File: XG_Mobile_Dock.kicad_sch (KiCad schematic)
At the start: 24 parts, among them J1 5-1775443-8, J2 20455-040E-76, J3 20455-040E-76, J4 3-2362375-4, J7 Conn_02x10_Odd_Even, J8 Conn_02x10_Odd_Even

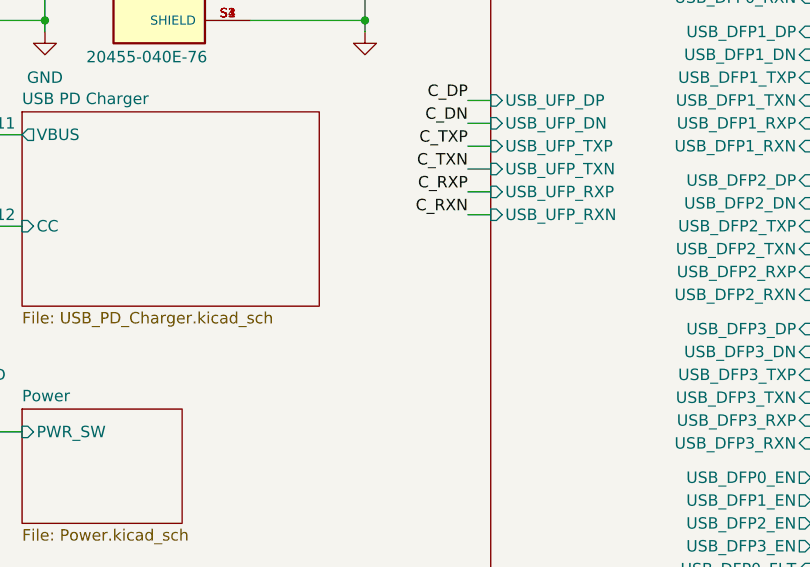
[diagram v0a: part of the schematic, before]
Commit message: Add TPS65987D charger circuit
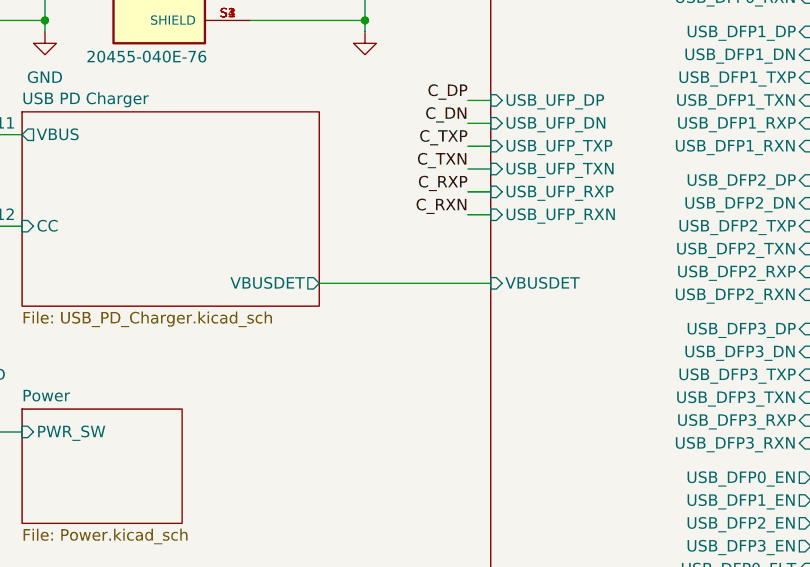
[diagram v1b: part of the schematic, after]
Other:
- sheet USB Hub ports: added VBUSDET; removed none
- sheet USB PD Charger ports: added VBUSDET; removed none
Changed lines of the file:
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@@
 	(wire
 		(pts
+			(xy 77.47 152.4) (xy 96.52 152.4)
+		)
+		(stroke
+			(width 0)
+			(type default)
+		)
+	)
+	(wire
+		(pts
 			(xy 82.55 123.19) (xy 82.55 124.46)
 		)
@@
 			)
 		)
+		(pin "VBUSDET" input
+			(at 96.52 152.4 180)
+			(effects
+				(font
+					(size 1.27 1.27)
+				)
+				(justify left)
+			)
+		)
 		(instances
 			(project "XG_Mobile_Dock"
@@
 			)
 		)
+		(pin "VBUSDET" output
+			(at 77.47 152.4 0)
+			(effects
+				(font
+					(size 1.27 1.27)
+				)
+				(justify right)
+			)
+		)

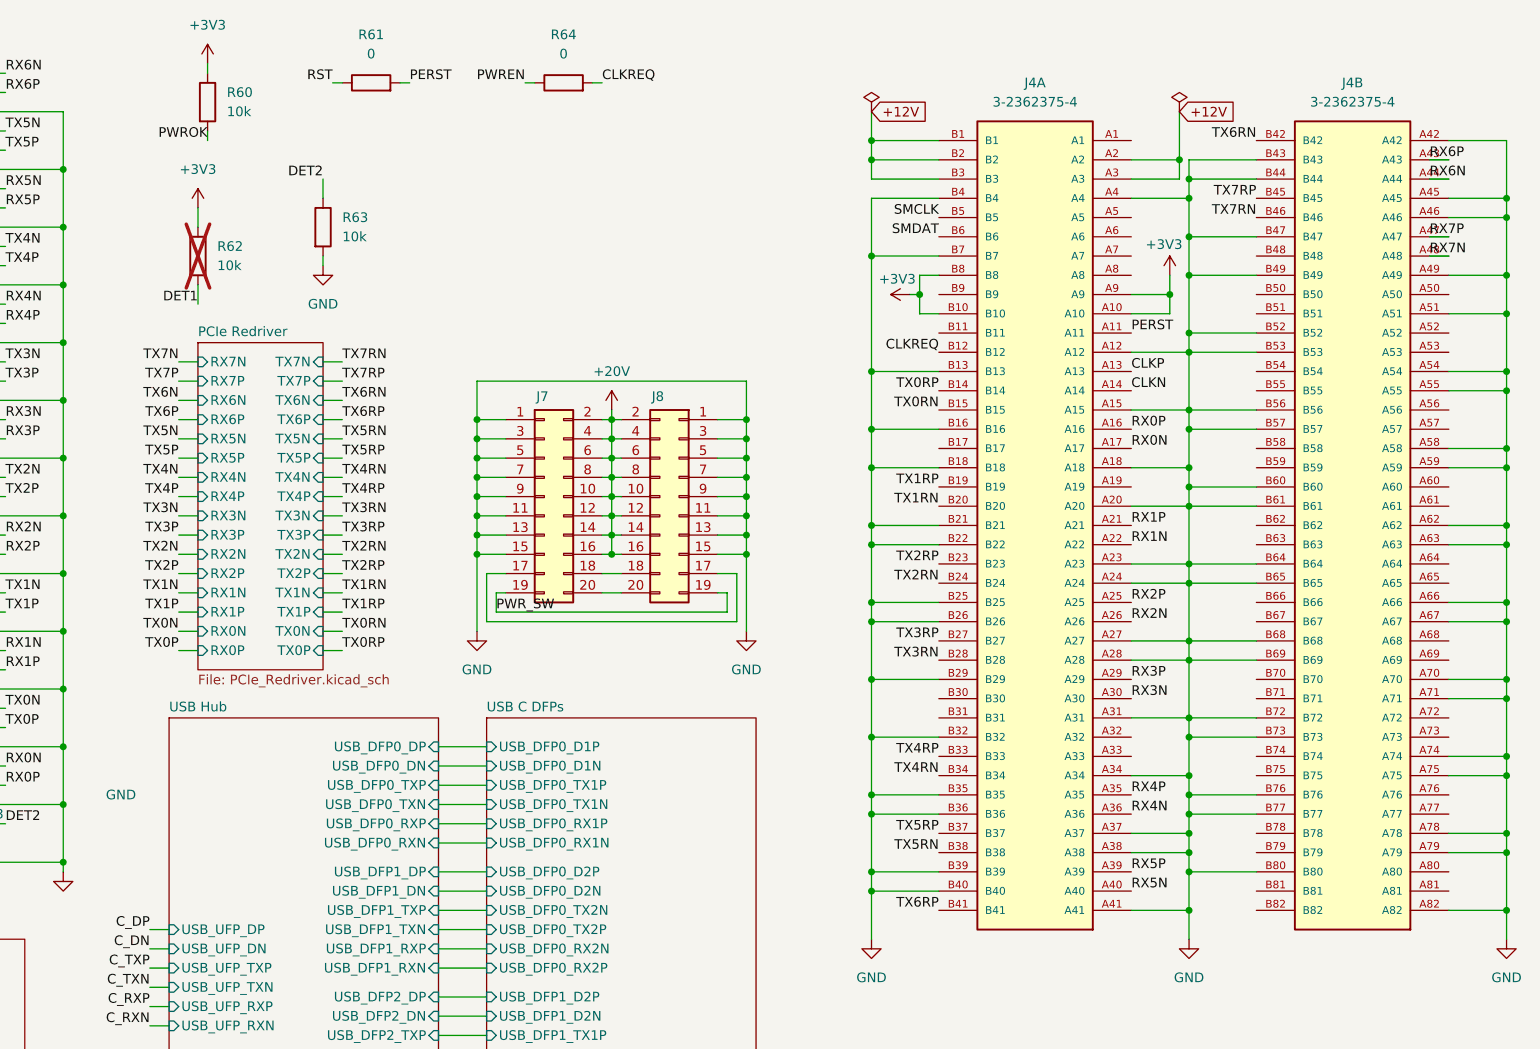
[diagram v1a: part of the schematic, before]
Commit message: Rewired PCIe without redriver
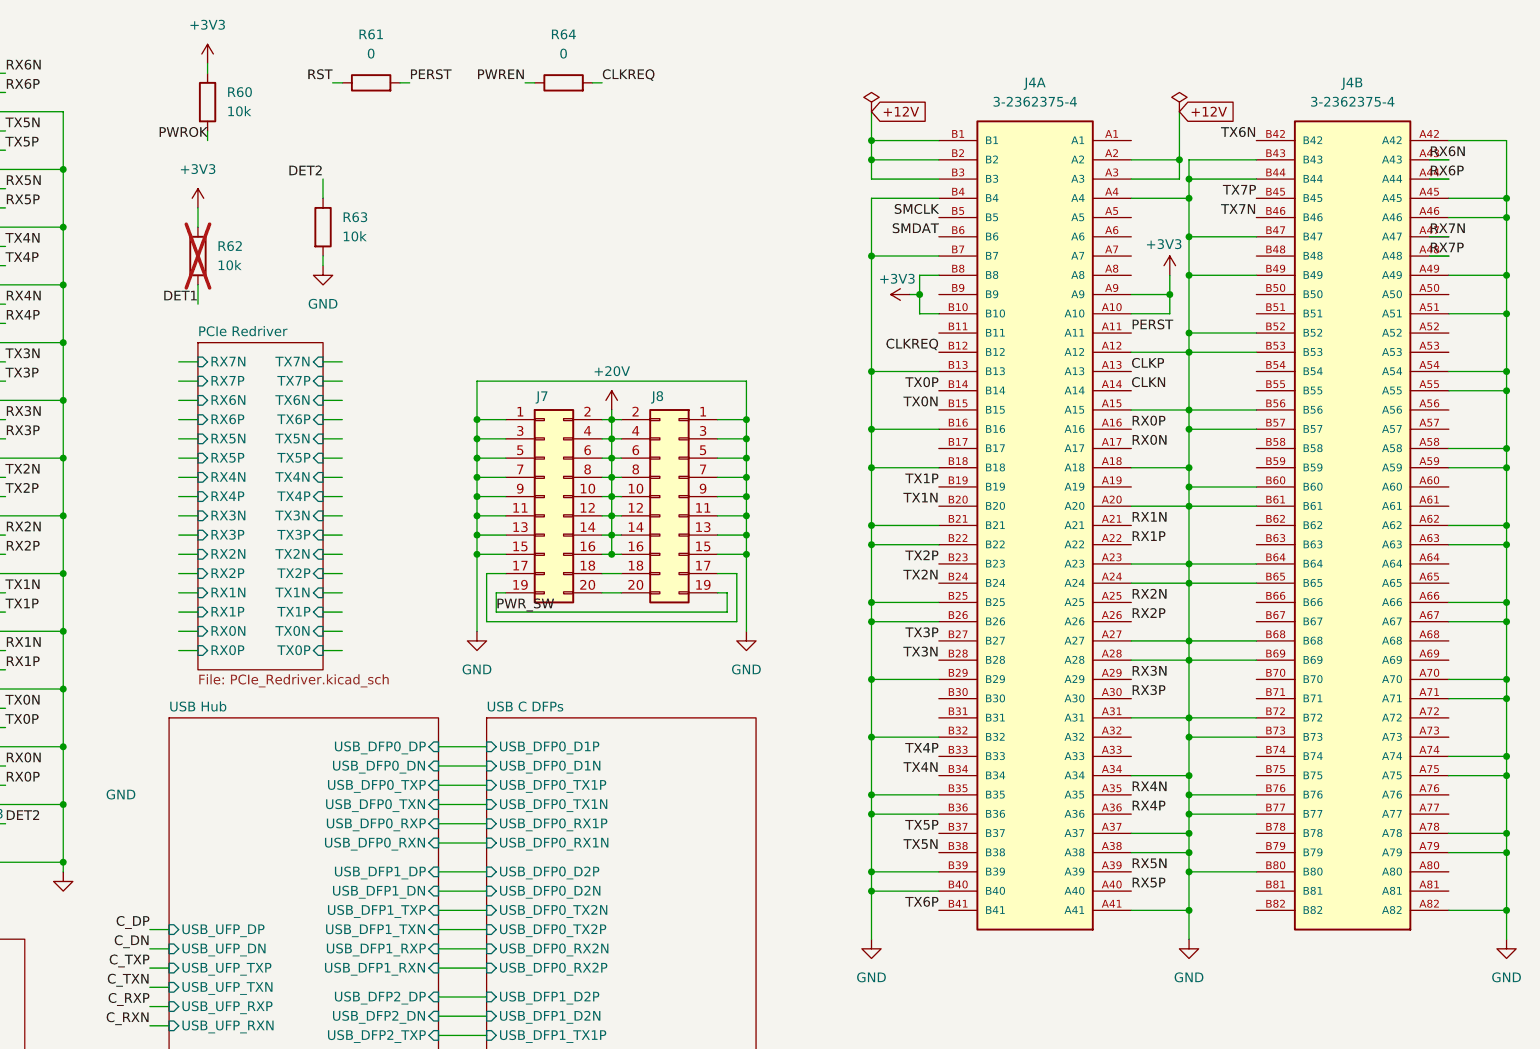
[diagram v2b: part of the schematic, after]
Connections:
- net TX0RN is gone; now on net TX0N: J4.B15
- net TX0RP is gone; now on net TX0P: J4.B14
- net TX1RN is gone; now on net TX1N: J4.B20
- net TX1RP is gone; now on net TX1P: J4.B19
- net TX2RN is gone; now on net TX2N: J4.B24
- net TX2RP is gone; now on net TX2P: J4.B23
- net TX3RN is gone; now on net TX3N: J4.B28
- net TX3RP is gone; now on net TX3P: J4.B27
- net TX4RN is gone; now on net TX4N: J4.B34
- net TX4RP is gone; now on net TX4P: J4.B33
- net TX5RN is gone; now on net TX5N: J4.B38
- net TX5RP is gone; now on net TX5P: J4.B37
- net TX6RN is gone; now on net TX6N: J4.B42
- net TX6RP is gone; now on net TX6P: J4.B41
- net TX7RN is gone; now on net TX7N: J4.B46
- net TX7RP is gone; now on net TX7P: J4.B45
- net RX1N: now also J4.A21; no longer J4.A22
- net RX1P: now also J4.A22; no longer J4.A21
- net RX2N: now also J4.A25; no longer J4.A26
- net RX2P: now also J4.A26; no longer J4.A25
- net RX3N: now also J4.A29; no longer J4.A30
- net RX3P: now also J4.A30; no longer J4.A29
- net RX4N: now also J4.A35; no longer J4.A36
- net RX4P: now also J4.A36; no longer J4.A35
- net RX5N: now also J4.A39; no longer J4.A40
- net RX5P: now also J4.A40; no longer J4.A39
- net RX6N: now also J4.A43; no longer J4.A44
- net RX6P: now also J4.A44; no longer J4.A43
- net RX7N: now also J4.A47; no longer J4.A48
- net RX7P: now also J4.A48; no longer J4.A47

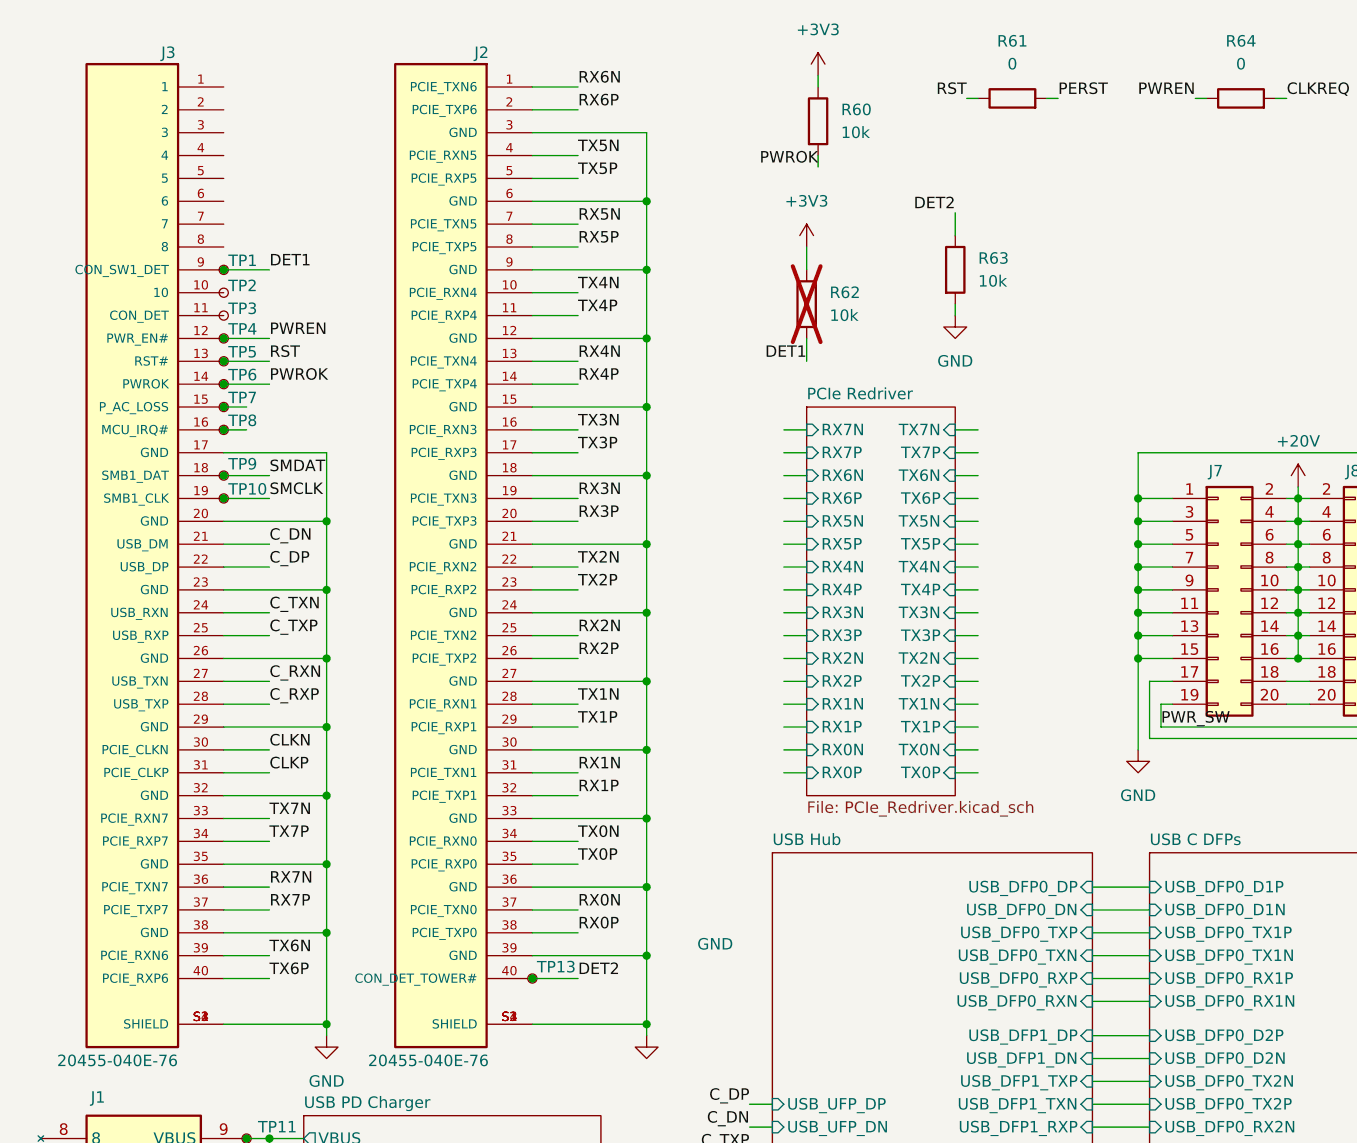
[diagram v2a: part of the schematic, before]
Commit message: Renamed some connector pins
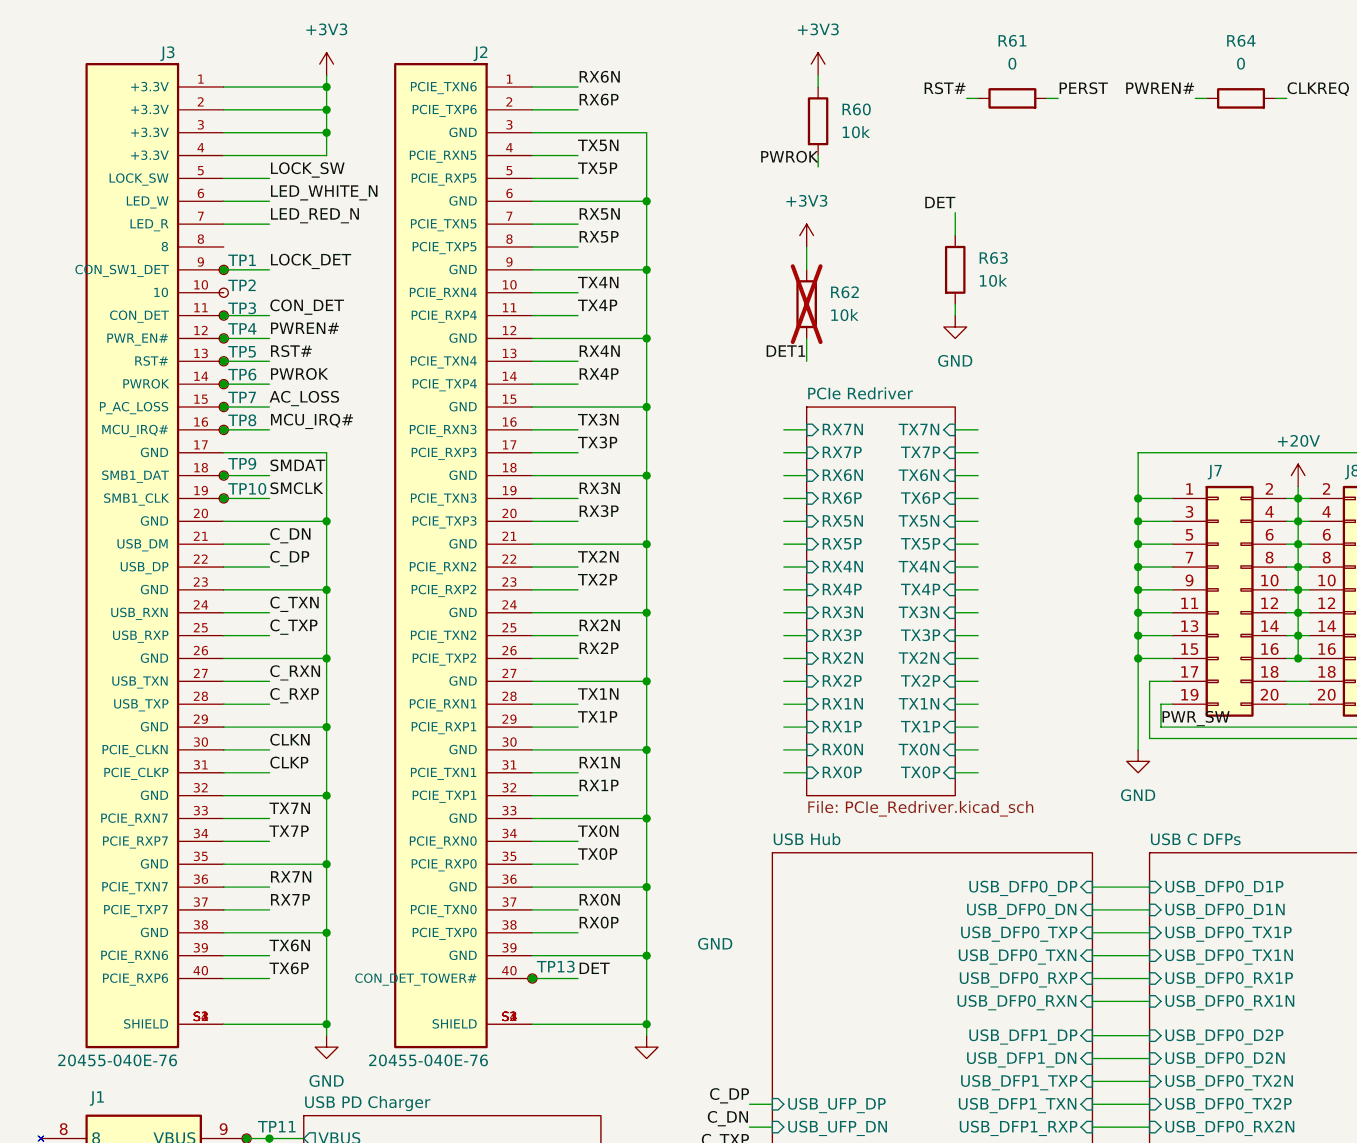
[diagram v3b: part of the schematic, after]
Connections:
- net +3V3: now also J3.1 (+3.3V), J3.2 (+3.3V), J3.3 (+3.3V), J3.4 (+3.3V)
- net DET1: no longer J3.9 (CON_SW1_DET), TP1.1
- net CON_DET: now reaches J3.11 (CON_DET), TP3.1
- net AC_LOSS: now reaches J3.15 (P_AC_LOSS), TP7.1
- net MCU_IRQ#: now reaches J3.16 (MCU_IRQ#), TP8.1
- net LOCK_SW: now reaches J3.5 (LOCK_SW)
- net LED_WHITE_N: now reaches J3.6 (LED_W)
- net LED_RED_N: now reaches J3.7 (LED_R)
- net DET2 renamed DET
- net PWREN renamed PWREN#
- net RST renamed RST#
- new net LOCK_DET: J3.9 (CON_SW1_DET), TP1.1
